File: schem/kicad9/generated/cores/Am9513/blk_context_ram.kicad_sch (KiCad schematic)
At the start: 0 parts

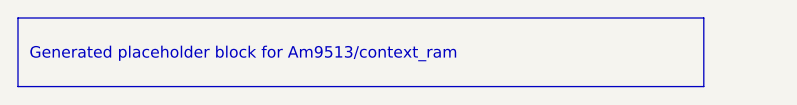
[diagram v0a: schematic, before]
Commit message: kicad: generate core-level hierarchical schematics
Detailed description:
- What changed: regenerated common and core schematics for Z85/Z90/Z380/Z480, Am9513/4/5, Am95xx, and CarbonIO/DMA placeholders
- Why it changed: update generated KiCad 9 outputs to reflect the final naming and tier model
- Files/paths affected: schem/kicad9/generated/common/* and schem/kicad9/generated/cores/*
- How to run it: scripts/gen_kicad.sh (or python tools/kicadgen/src/kicadgen.py)
- What remains TODO: regenerate and commit system-level schematics
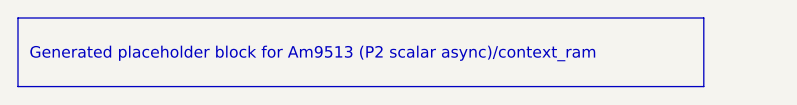
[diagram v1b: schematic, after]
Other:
- title: Am9513::context_ram -> Am9513 (P2 scalar async)::context_ram
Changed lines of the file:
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@@
 	(version 20250114)
 	(generator "kicadgen")
-	(generator_version "0.1")
+	(generator_version "0.2")
 	(paper "A3")
 	(title_block
-		(title "Am9513::context_ram")
+		(title "Am9513 (P2 scalar async)::context_ram")
 		(company "Project Carbon")
 		(comment 1 "Generated - do not edit in generated/")
@@
 	)
 	(text_box
-		"Generated placeholder block for Am9513/context_ram"
+		"Generated placeholder block for Am9513 (P2 scalar async)/context_ram"
 		(exclude_from_sim no)
 		(at
